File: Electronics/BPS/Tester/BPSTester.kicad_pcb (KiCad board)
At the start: 2 copper layers, 26 parts, among them J1 Conn_01x13_Male

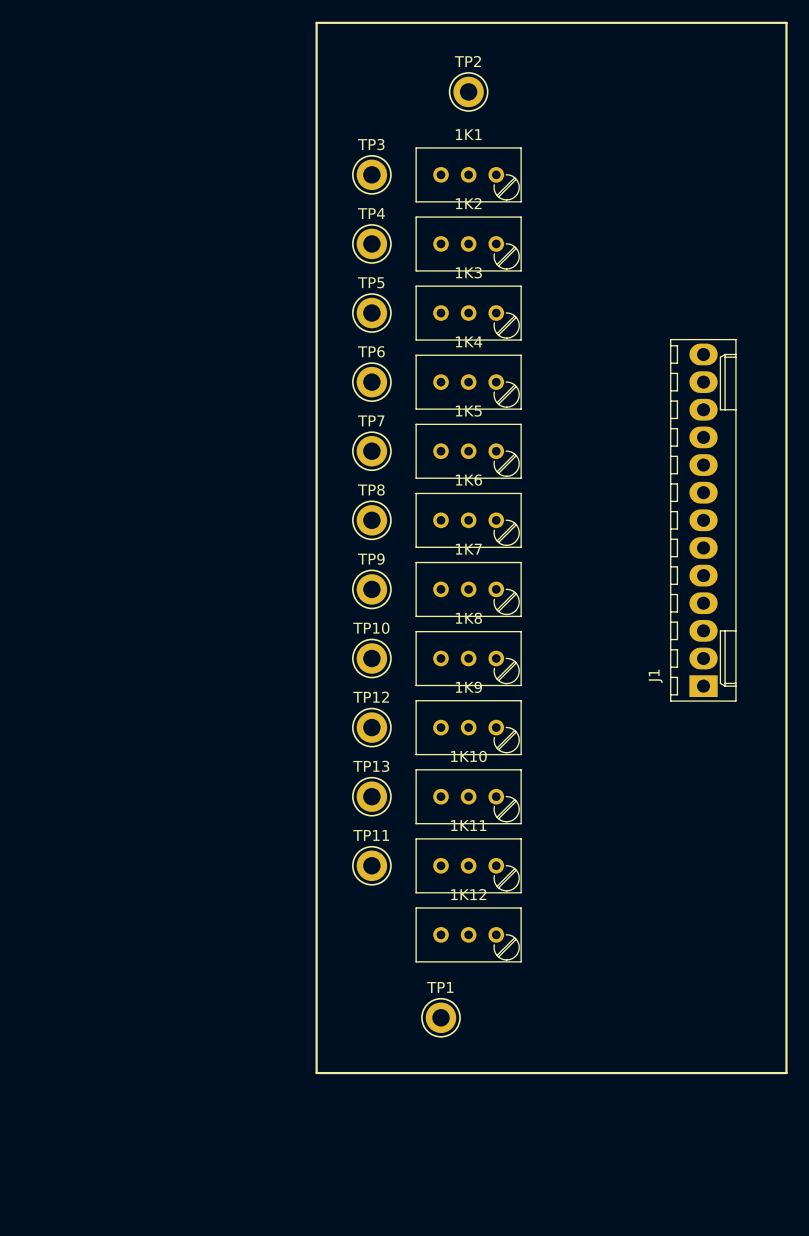
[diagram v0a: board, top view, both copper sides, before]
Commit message: routed the tracks, still need to follow design guidelines
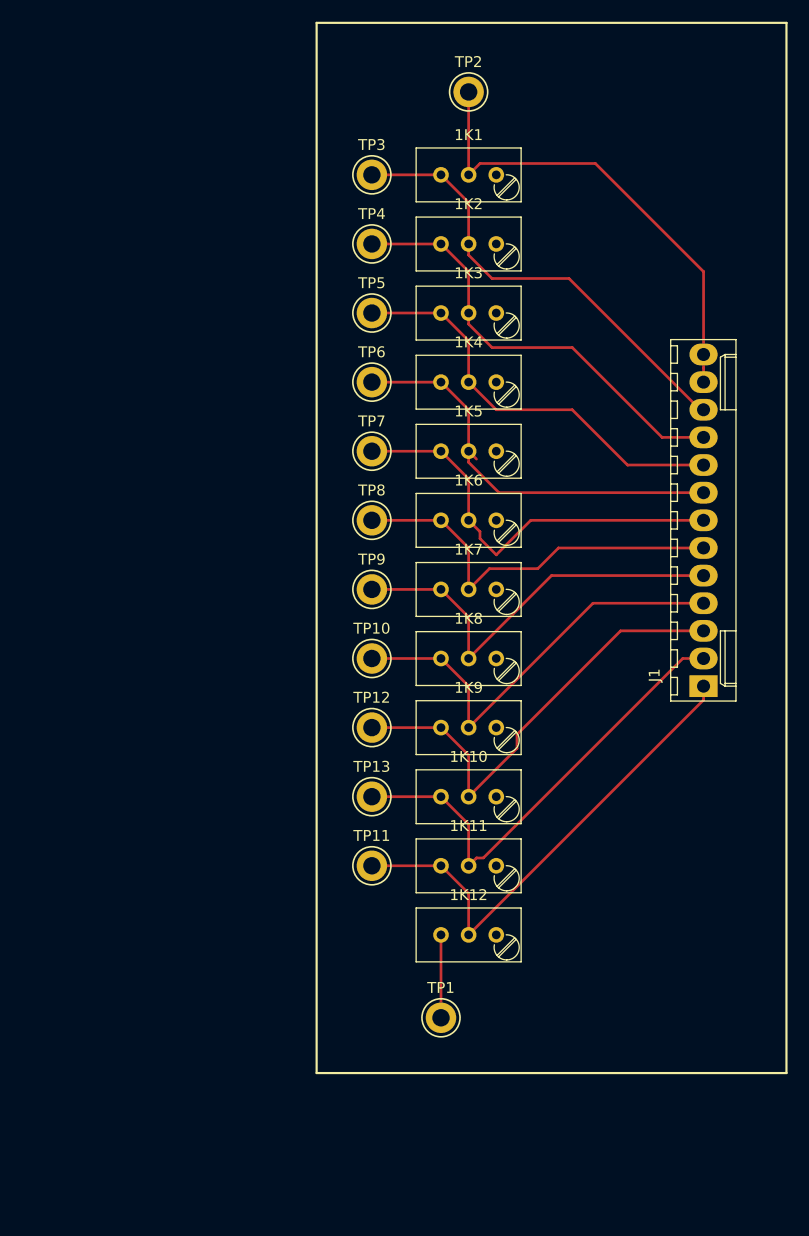
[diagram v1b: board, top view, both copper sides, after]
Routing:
- net Net-(1K11-Pad3): track 0.00 -> 45.6 mm
- net +BATT: track 0.00 -> 43.9 mm
- net Net-(1K10-Pad3): track 0.00 -> 43.2 mm
- net Net-(1K10-Pad2): track 0.00 -> 42.4 mm
- net Net-(1K1-Pad3): track 0.00 -> 42.3 mm
- net Net-(1K2-Pad3): track 0.00 -> 40.7 mm
- net Net-(1K8-Pad3): track 0.00 -> 40.1 mm
- net Net-(1K4-Pad3): track 0.00 -> 38.5 mm
- net Net-(1K7-Pad3): track 0.00 -> 38.5 mm
- net Net-(1K3-Pad3): track 0.00 -> 38.5 mm
- net Net-(1K5-Pad3): track 0.00 -> 38.3 mm
- net Net-(1K6-Pad3): track 0.00 -> 36.9 mm
- net GND: track 0.00 -> 7.62 mm
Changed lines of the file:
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@@
     (thickness 1.6)
     (drawings 4)
-    (tracks 0)
+    (tracks 82)
     (zones 0)
     (modules 26)
@@
     (solder_mask_min_width 0.25)
     (aux_axis_origin 0 0)
-    (visible_elements FFFFFF7F)
+    (visible_elements 7FFFFFFF)
     (pcbplotparams
       (layerselection 0x010fc_ffffffff)
@@
   (gr_line (start 127 137.16) (end 170.18 137.16) (layer F.SilkS) (width 0.2))
   (gr_line (start 127 40.64) (end 127 137.16) (layer F.SilkS) (width 0.2))
+  (segment (start 140.97 46.99) (end 140.97 54.61) (width 0.25) (layer F.Cu) (net 2))
+  (segment (start 142.015001 53.564999) (end 152.624999 53.564999) (width 0.25) (layer F.Cu) (net 2))
+  (segment (start 140.97 54.61) (end 142.015001 53.564999) (width 0.25) (layer F.Cu) (net 2))
+  (segment (start 162.56 63.5) (end 162.56 71.12) (width 0.25) (layer F.Cu) (net 2))
+  (segment (start 152.624999 53.564999) (end 162.56 63.5) (width 0.25) (layer F.Cu) (net 2))
+  (segment (start 162.56 72.37) (end 162.56 73.66) (width 0.25) (layer F.Cu) (net 2))
+  (segment (start 162.56 71.12) (end 162.56 72.37) (width 0.25) (layer F.Cu) (net 2))
+  (segment (start 132.08 54.61) (end 138.43 54.61) (width 0.25) (layer F.Cu) (net 3))
+  (segment (start 140.97 57.15) (end 140.97 60.96) (width 0.25) (layer F.Cu) (net 3))
+  (segment (start 138.43 54.61) (end 140.97 57.15) (width 0.25) (layer F.Cu) (net 3))
+  (segment (start 162.26 76.2) (end 162.56 76.2) (width 0.25) (layer F.Cu) (net 3))
+  (segment (start 150.195 64.135) (end 162.26 76.2) (width 0.25) (layer F.Cu) (net 3))
+  (segment (start 143.126767 64.135) (end 150.195 64.135) (width 0.25) (layer F.Cu) (net 3))
+  (segment (start 140.97 61.978233) (end 143.126767 64.135) (width 0.25) (layer F.Cu) (net 3))
+  (segment (start 140.97 60.96) (end 140.97 61.978233) (width 0.25) (layer F.Cu) (net 3))
+  (segment (start 132.08 60.96) (end 138.43 60.96) (width 0.25) (layer F.Cu) (net 4))
+  (segment (start 140.97 63.5) (end 140.97 67.31) (width 0.25) (layer F.Cu) (net 4))
+  (segment (start 138.43 60.96) (end 140.97 63.5) (width 0.25) (layer F.Cu) (net 4))
+  (segment (start 140.97 68.328233) (end 143.126767 70.485) (width 0.25) (layer F.Cu) (net 4))
+  (segment (start 140.97 67.31) (end 140.97 68.328233) (width 0.25) (layer F.Cu) (net 4))
+  (segment (start 143.126767 70.485) (end 150.495 70.485) (width 0.25) (layer F.Cu) (net 4))
+  (segment (start 158.75 78.74) (end 162.56 78.74) (width 0.25) (layer F.Cu) (net 4))
+  (segment (start 150.495 70.485) (end 158.75 78.74) (width 0.25) (layer F.Cu) (net 4))
+  (segment (start 132.08 67.31) (end 138.43 67.31) (width 0.25) (layer F.Cu) (net 7))
+  (segment (start 138.43 67.31) (end 140.97 69.85) (width 0.25) (layer F.Cu) (net 7))
+  (segment (start 140.97 69.85) (end 140.97 73.66) (width 0.25) (layer F.Cu) (net 7))
+  (segment (start 140.97 73.66) (end 143.51 76.2) (width 0.25) (layer F.Cu) (net 7))
+  (segment (start 143.51 76.2) (end 150.495 76.2) (width 0.25) (layer F.Cu) (net 7))
+  (segment (start 155.575 81.28) (end 162.56 81.28) (width 0.25) (layer F.Cu) (net 7))
+  (segment (start 150.495 76.2) (end 155.575 81.28) (width 0.25) (layer F.Cu) (net 7))
+  (segment (start 132.08 73.66) (end 138.43 73.66) (width 0.25) (layer F.Cu) (net 8))
+  (segment (start 138.43 73.66) (end 140.97 76.2) (width 0.25) (layer F.Cu) (net 8))
+  (segment (start 140.97 76.2) (end 140.97 80.01) (width 0.25) (layer F.Cu) (net 8))
+  (segment (start 140.97 80.01) (end 141.689999 80.729999) (width 0.25) (layer F.Cu) (net 8))
+  (segment (start 143.761767 83.82) (end 162.56 83.82) (width 0.25) (layer F.Cu) (net 8))
+  (segment (start 140.97 80.01) (end 140.97 81.028233) (width 0.25) (layer F.Cu) (net 8))
+  (segment (start 140.97 81.028233) (end 143.761767 83.82) (width 0.25) (layer F.Cu) (net 8))
+  (segment (start 132.08 80.01) (end 138.43 80.01) (width 0.25) (layer F.Cu) (net 11))
+  (segment (start 140.97 82.55) (end 140.97 86.36) (width 0.25) (layer F.Cu) (net 11))
+  (segment (start 138.43 80.01) (end 140.97 82.55) (width 0.25) (layer F.Cu) (net 11))
+  (segment (start 146.685 86.36) (end 162.56 86.36) (width 0.25) (layer F.Cu) (net 11))
+  (segment (start 143.51 89.535) (end 146.685 86.36) (width 0.25) (layer F.Cu) (net 11))
+  (segment (start 142.015001 88.040001) (end 143.51 89.535) (width 0.25) (layer F.Cu) (net 11))
+  (segment (start 140.97 86.36) (end 142.015001 87.405001) (width 0.25) (layer F.Cu) (net 11))
+  (segment (start 142.015001 87.405001) (end 142.015001 88.040001) (width 0.25) (layer F.Cu) (net 11))
+  (segment (start 132.08 86.36) (end 138.43 86.36) (width 0.25) (layer F.Cu) (net 12))
+  (segment (start 138.43 86.36) (end 140.97 88.9) (width 0.25) (layer F.Cu) (net 12))
+  (segment (start 140.97 88.9) (end 140.97 92.71) (width 0.25) (layer F.Cu) (net 12))
+  (segment (start 149.225 88.9) (end 162.56 88.9) (width 0.25) (layer F.Cu) (net 12))
+  (segment (start 147.32 90.805) (end 149.225 88.9) (width 0.25) (layer F.Cu) (net 12))
+  (segment (start 140.97 92.71) (end 142.875 90.805) (width 0.25) (layer F.Cu) (net 12))
+  (segment (start 142.875 90.805) (end 147.32 90.805) (width 0.25) (layer F.Cu) (net 12))
+  (segment (start 132.08 92.71) (end 138.43 92.71) (width 0.25) (layer F.Cu) (net 15))
+  (segment (start 140.97 95.25) (end 140.97 99.06) (width 0.25) (layer F.Cu) (net 15))
+  (segment (start 138.43 92.71) (end 140.97 95.25) (width 0.25) (layer F.Cu) (net 15))
+  (segment (start 148.59 91.44) (end 162.56 91.44) (width 0.25) (layer F.Cu) (net 15))
+  (segment (start 140.97 99.06) (end 148.59 91.44) (width 0.25) (layer F.Cu) (net 15))
+  (segment (start 132.08 99.06) (end 138.43 99.06) (width 0.25) (layer F.Cu) (net 16))
+  (segment (start 138.43 99.06) (end 140.97 101.6) (width 0.25) (layer F.Cu) (net 16))
+  (segment (start 140.97 101.6) (end 140.97 105.41) (width 0.25) (layer F.Cu) (net 16))
+  (segment (start 152.4 93.98) (end 162.56 93.98) (width 0.25) (layer F.Cu) (net 16))
+  (segment (start 140.97 105.41) (end 152.4 93.98) (width 0.25) (layer F.Cu) (net 16))
+  (segment (start 132.08 105.41) (end 138.43 105.41) (width 0.25) (layer F.Cu) (net 19))
+  (segment (start 140.97 107.95) (end 140.97 111.76) (width 0.25) (layer F.Cu) (net 19))
+  (segment (start 138.43 105.41) (end 140.97 107.95) (width 0.25) (layer F.Cu) (net 19))
+  (segment (start 140.97 111.76) (end 145.415 107.315) (width 0.25) (layer F.Cu) (net 19))
+  (segment (start 145.415 107.315) (end 145.415 106.045) (width 0.25) (layer F.Cu) (net 19))
+  (segment (start 154.94 96.52) (end 162.56 96.52) (width 0.25) (layer F.Cu) (net 19))
+  (segment (start 145.415 106.045) (end 154.94 96.52) (width 0.25) (layer F.Cu) (net 19))
+  (segment (start 132.08 111.76) (end 138.43 111.76) (width 0.25) (layer F.Cu) (net 20))
+  (segment (start 140.97 114.3) (end 140.97 118.11) (width 0.25) (layer F.Cu) (net 20))
+  (segment (start 138.43 111.76) (end 140.97 114.3) (width 0.25) (layer F.Cu) (net 20))
+  (segment (start 160.655 99.06) (end 162.56 99.06) (width 0.25) (layer F.Cu) (net 20))
+  (segment (start 142.324999 117.390001) (end 160.655 99.06) (width 0.25) (layer F.Cu) (net 20))
+  (segment (start 140.97 118.11) (end 141.689999 117.390001) (width 0.25) (layer F.Cu) (net 20))
+  (segment (start 141.689999 117.390001) (end 142.324999 117.390001) (width 0.25) (layer F.Cu) (net 20))
+  (segment (start 132.08 118.11) (end 138.43 118.11) (width 0.25) (layer F.Cu) (net 23))
+  (segment (start 138.43 118.11) (end 140.97 120.65) (width 0.25) (layer F.Cu) (net 23))
+  (segment (start 140.97 120.65) (end 140.97 124.46) (width 0.25) (layer F.Cu) (net 23))
+  (segment (start 162.56 102.87) (end 162.56 101.6) (width 0.25) (layer F.Cu) (net 23))
+  (segment (start 140.97 124.46) (end 162.56 102.87) (width 0.25) (layer F.Cu) (net 23))
+  (segment (start 138.43 124.46) (end 138.43 132.08) (width 0.25) (layer F.Cu) (net 24))
 )

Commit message: Changed the track with to 15 mil
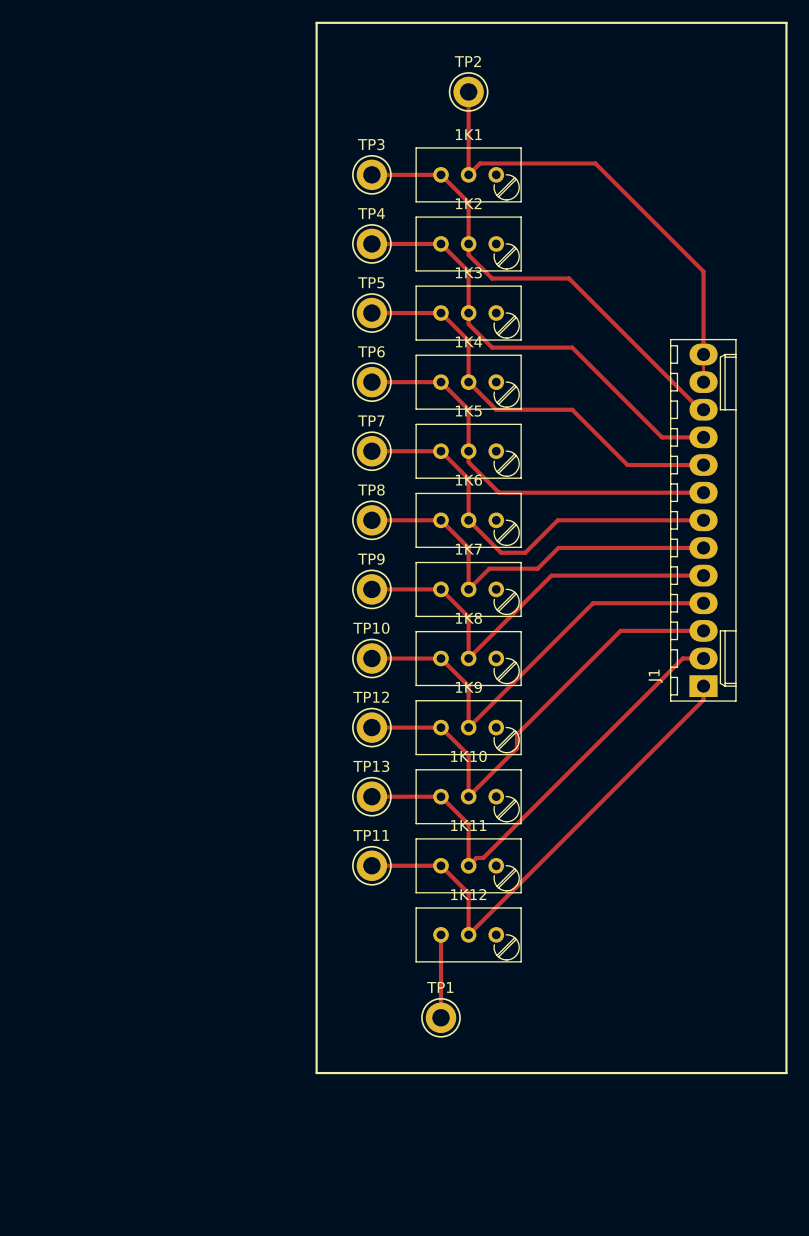
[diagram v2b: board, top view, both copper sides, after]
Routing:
- net Net-(1K4-Pad3): track 38.5 -> 37.5 mm
- net Net-(1K5-Pad3): track 38.3 -> 37.8 mm
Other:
- net class Default: clearance 0.2 -> 0.1524; trace_width 0.25 -> 0.3048; via_dia 0.8 -> 0.762; via_drill 0.4 -> 0.381
- rule trace_clearance: 0.2 -> 0.1524
